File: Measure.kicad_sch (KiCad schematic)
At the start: 22 parts, among them U4 AD8210, U5 AD8210, U6 AD8210, U7 AD8210

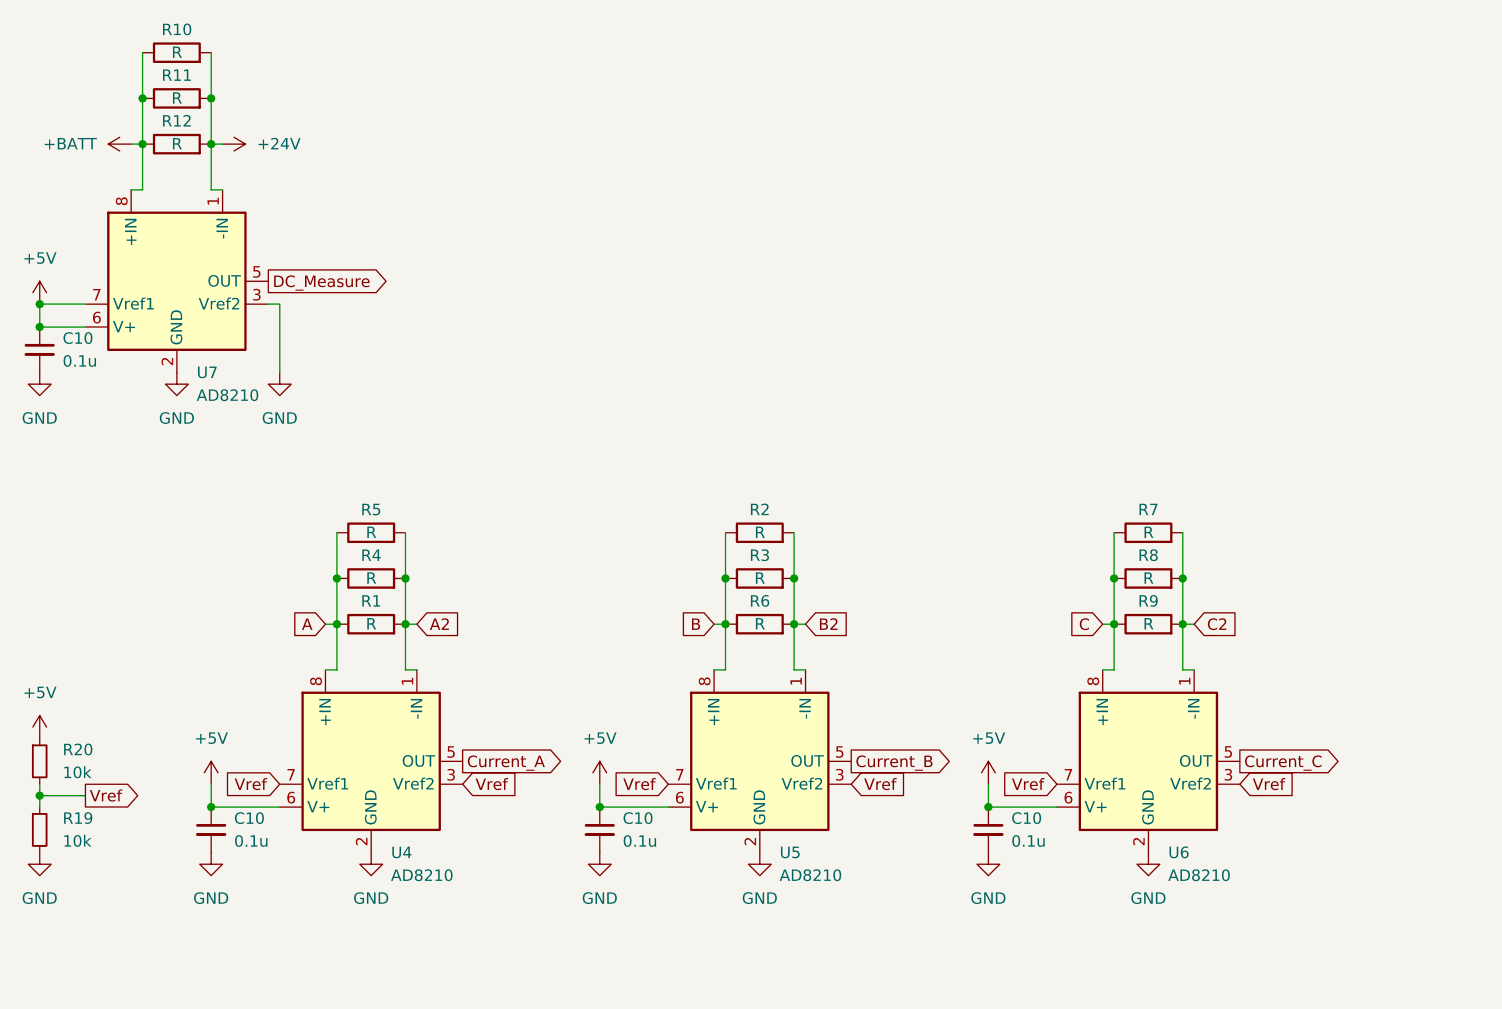
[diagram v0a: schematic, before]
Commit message: Добавил шунты
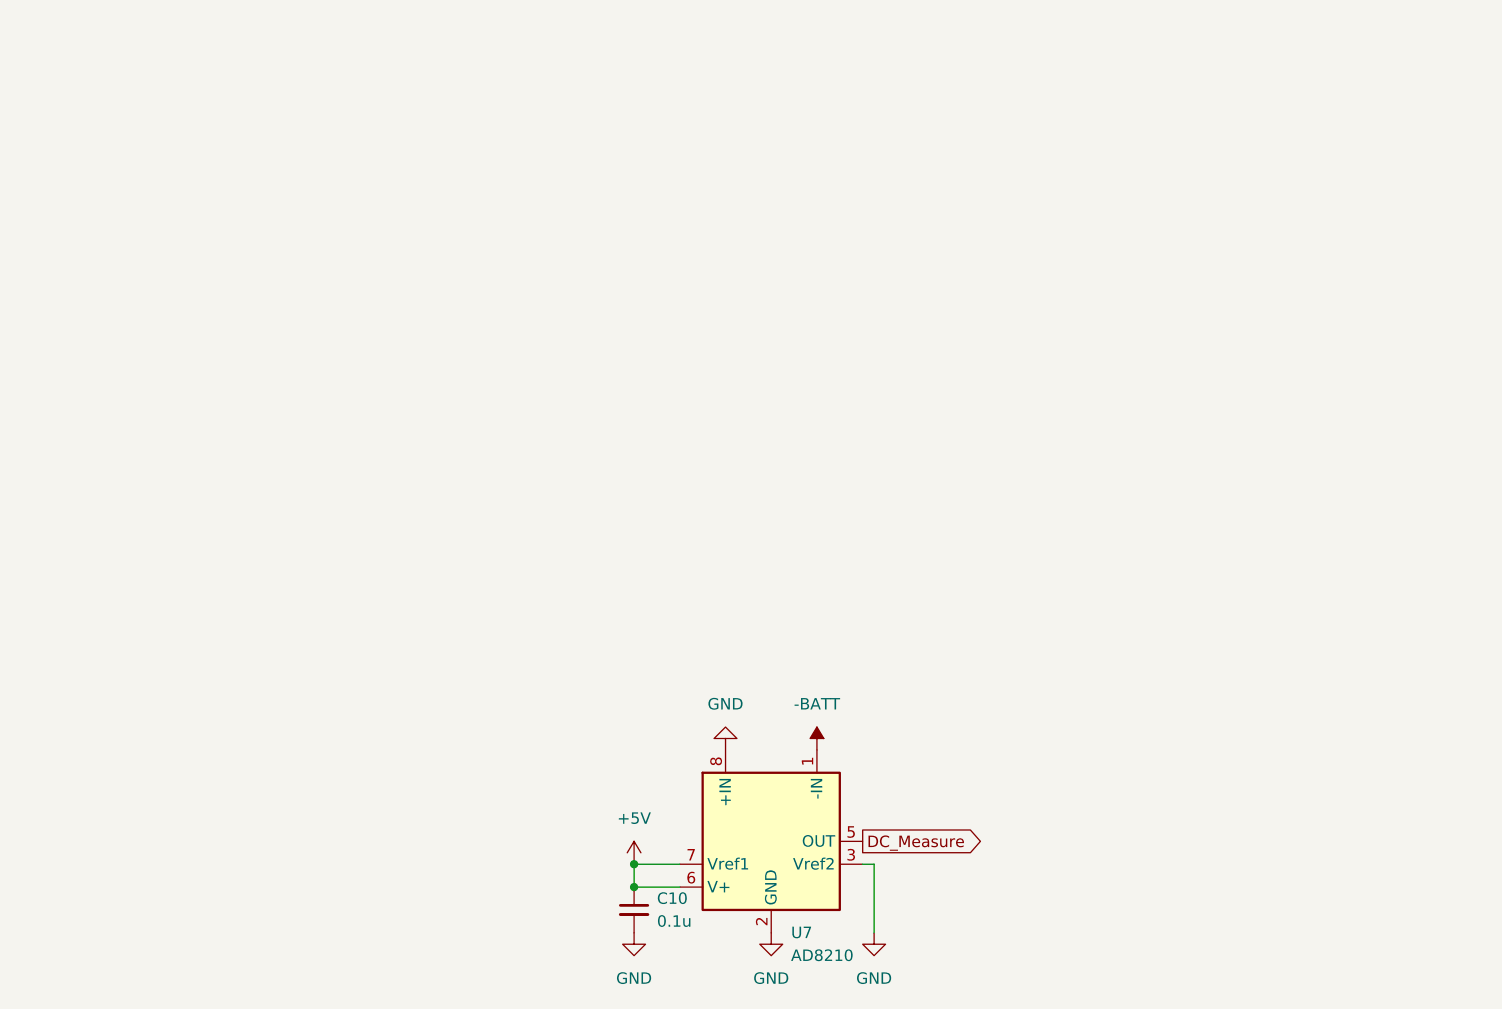
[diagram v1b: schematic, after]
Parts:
- removed C10 (x3): 0.1u, Capacitor_SMD:C_0805_2012Metric_Pad1.18x1.45mm_HandSolder, symbol Device:C_Small
- removed R1, R10, R11, R12, R2, R3, R4, R5, R6, R7, R8, R9: R, Resistor_SMD:R_2512_6332Metric_Pad1.40x3.35mm_HandSolder, symbol Device:R
- removed R19, R20: 10k, Resistor_SMD:R_0805_2012Metric_Pad1.20x1.40mm_HandSolder, symbol Device:R_Small
- removed U4, U5, U6: AD8210, Package_SO:SOIC-8_3.9x4.9mm_P1.27mm, symbol Amplifier_Current:AD8210
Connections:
- net +BATT is gone; now on net GND: U7.8 (+IN)
- net +24V renamed -BATT
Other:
- moved on the sheet: C10, U7

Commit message: Стартовый вариант
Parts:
- added C10: 0.1u, Capacitor_SMD:C_0805_2012Metric_Pad1.18x1.45mm_HandSolder, symbol Device:C_Small
- added C10 (x2): 56p, Capacitor_SMD:C_0805_2012Metric_Pad1.18x1.45mm_HandSolder, symbol Device:C_Small
- added R2, R3, R4, R5: 120, Resistor_SMD:R_0805_2012Metric_Pad1.20x1.40mm_HandSolder, symbol Device:R_Small
- added U1: LMV7239M5, Package_TO_SOT_SMD:SOT-353_SC-70-5, symbol Comparator:LMV7219M7
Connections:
- net +5V: now also C10.1, R3.2, U1.5 (V+)
- net DC_Measure: now also R5.2
- net GND: now also C10.2, C10.2, C10.2, R4.1, U1.2 (V-); no longer U7.8 (+IN)
- net -BATT renamed Shunt_2
- new net: C10.1, R5.1, U1.4 (-)
- new net: R3.1, R4.2, U1.3 (+)
- new net: R2.1, U1.1
- new net Enable: C10.1, R2.2
- new net Shunt_1: U7.8 (+IN)

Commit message: Стартовая версия
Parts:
- removed C10: 0.1u, Capacitor_SMD:C_0805_2012Metric_Pad1.18x1.45mm_HandSolder, symbol Device:C_Small
- removed C10: 56p, Capacitor_SMD:C_0805_2012Metric_Pad1.18x1.45mm_HandSolder, symbol Device:C_Small
- removed R2, R3, R4: 120, Resistor_SMD:R_0805_2012Metric_Pad1.20x1.40mm_HandSolder, symbol Device:R_Small
- removed U1: LMV7239M5, Package_TO_SOT_SMD:SOT-353_SC-70-5, symbol Comparator:LMV7219M7
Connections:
- net DC_Measure: now also C10.1, R5.1; no longer R5.2, U7.5 (OUT)
- new net: R5.2, U7.5 (OUT)
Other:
- moved on the sheet: R5

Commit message: Стартовая версия
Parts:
- renumbered R5 to R9
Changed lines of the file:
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@@
   (symbol (lib_id "Device:R_Small") (at 121.92 110.49 270) (unit 1)
     (in_bom yes) (on_board yes) (dnp no) (fields_autoplaced)
-    (property "Reference" "R5" (at 121.92 105.41 90)
+    (property "Reference" "R9" (at 121.92 105.41 90)
       (effects (font (size 1.27 1.27)))
     )
@@
       (project "Силовая плата"
         (path "/96c6fc92-8ec6-44f7-b0dc-9ad8f1acea09/1efb5faf-bb82-4ac6-a144-d6576b4720aa"
-          (reference "R5") (unit 1)
+          (reference "R9") (unit 1)
         )
       )
@@
         )
         (path "/96c6fc92-8ec6-44f7-b0dc-9ad8f1acea09/1efb5faf-bb82-4ac6-a144-d6576b4720aa"
-          (reference "U6") (unit 1)
+          (reference "U1") (unit 1)
         )
         (path "/96c6fc92-8ec6-44f7-b0dc-9ad8f1acea09/a27b443f-c036-4fd6-934c-6ea912709de0"
@@
         )
         (path "/96c6fc92-8ec6-44f7-b0dc-9ad8f1acea09/1efb5faf-bb82-4ac6-a144-d6576b4720aa"
-          (reference "C10") (unit 1)
+          (reference "C2") (unit 1)
         )
         (path "/96c6fc92-8ec6-44f7-b0dc-9ad8f1acea09/a27b443f-c036-4fd6-934c-6ea912709de0"
@@
         )
         (path "/96c6fc92-8ec6-44f7-b0dc-9ad8f1acea09/1efb5faf-bb82-4ac6-a144-d6576b4720aa"
-          (reference "C12") (unit 1)
+          (reference "C3") (unit 1)
         )
         (path "/96c6fc92-8ec6-44f7-b0dc-9ad8f1acea09/a27b443f-c036-4fd6-934c-6ea912709de0"
@@
         )
         (path "/96c6fc92-8ec6-44f7-b0dc-9ad8f1acea09/1efb5faf-bb82-4ac6-a144-d6576b4720aa"
+          (reference "#PWR09") (unit 1)
+        )
+        (path "/96c6fc92-8ec6-44f7-b0dc-9ad8f1acea09/a27b443f-c036-4fd6-934c-6ea912709de0"
+          (reference "#PWR029") (unit 1)
+        )
+      )
+    )
+  )
+  (symbol (lib_id "power:GND") (at 88.9 120.65 0) (unit 1)
+    (in_bom yes) (on_board yes) (dnp no) (fields_autoplaced)
+    (property "Reference" "#PWR011" (at 88.9 127 0)
+      (effects (font (size 1.27 1.27)) hide)
+    )
+    (property "Value" "GND" (at 88.9 125.73 0)
+      (effects (font (size 1.27 1.27)))
+    )
+    (property "Footprint" "" (at 88.9 120.65 0)
+      (effects (font (size 1.27 1.27)) hide)
+    )
+    (property "Datasheet" "" (at 88.9 120.65 0)
+      (effects (font (size 1.27 1.27)) hide)
+    )
+    (pin "1")
+    (instances
+      (project "Силовая плата"
+        (path "/96c6fc92-8ec6-44f7-b0dc-9ad8f1acea09"
+          (reference "#PWR011") (unit 1)
+        )
+        (path "/96c6fc92-8ec6-44f7-b0dc-9ad8f1acea09/1efb5faf-bb82-4ac6-a144-d6576b4720aa"
+          (reference "#PWR07") (unit 1)
+        )
+        (path "/96c6fc92-8ec6-44f7-b0dc-9ad8f1acea09/a27b443f-c036-4fd6-934c-6ea912709de0"
+          (reference "#PWR021") (unit 1)
+        )
+      )
+    )
+  )
+  (symbol (lib_id "power:GND") (at 129.54 120.65 0) (unit 1)
+    (in_bom yes) (on_board yes) (dnp no) (fields_autoplaced)
+    (property "Reference" "#PWR06" (at 129.54 127 0)
+      (effects (font (size 1.27 1.27)) hide)
+    )
+    (property "Value" "GND" (at 129.54 125.73 0)
+      (effects (font (size 1.27 1.27)))
+    )
+    (property "Footprint" "" (at 129.54 120.65 0)
+      (effects (font (size 1.27 1.27)) hide)
+    )
+    (property "Datasheet" "" (at 129.54 120.65 0)
+      (effects (font (size 1.27 1.27)) hide)
+    )
+    (pin "1")
+    (instances
+      (project "Силовая плата"
+        (path "/96c6fc92-8ec6-44f7-b0dc-9ad8f1acea09"
+          (reference "#PWR06") (unit 1)
+        )
+        (path "/96c6fc92-8ec6-44f7-b0dc-9ad8f1acea09/1efb5faf-bb82-4ac6-a144-d6576b4720aa"
           (reference "#PWR010") (unit 1)
         )
         (path "/96c6fc92-8ec6-44f7-b0dc-9ad8f1acea09/a27b443f-c036-4fd6-934c-6ea912709de0"
-          (reference "#PWR029") (unit 1)
-        )
-      )
-    )
-  )
-  (symbol (lib_id "power:GND") (at 88.9 120.65 0) (unit 1)
-    (in_bom yes) (on_board yes) (dnp no) (fields_autoplaced)
-    (property "Reference" "#PWR011" (at 88.9 127 0)
-      (effects (font (size 1.27 1.27)) hide)
-    )
-    (property "Value" "GND" (at 88.9 125.73 0)
-      (effects (font (size 1.27 1.27)))
-    )
-    (property "Footprint" "" (at 88.9 120.65 0)
-      (effects (font (size 1.27 1.27)) hide)
-    )
-    (property "Datasheet" "" (at 88.9 120.65 0)
-      (effects (font (size 1.27 1.27)) hide)
-    )
-    (pin "1")
-    (instances
-      (project "Силовая плата"
-        (path "/96c6fc92-8ec6-44f7-b0dc-9ad8f1acea09"
-          (reference "#PWR011") (unit 1)
-        )
-        (path "/96c6fc92-8ec6-44f7-b0dc-9ad8f1acea09/1efb5faf-bb82-4ac6-a144-d6576b4720aa"
-          (reference "#PWR04") (unit 1)
-        )
-        (path "/96c6fc92-8ec6-44f7-b0dc-9ad8f1acea09/a27b443f-c036-4fd6-934c-6ea912709de0"
-          (reference "#PWR021") (unit 1)
-        )
-      )
-    )
-  )
-  (symbol (lib_id "power:GND") (at 129.54 120.65 0) (unit 1)
-    (in_bom yes) (on_board yes) (dnp no) (fields_autoplaced)
-    (property "Reference" "#PWR06" (at 129.54 127 0)
-      (effects (font (size 1.27 1.27)) hide)
-    )
-    (property "Value" "GND" (at 129.54 125.73 0)
-      (effects (font (size 1.27 1.27)))
-    )
-    (property "Footprint" "" (at 129.54 120.65 0)
-      (effects (font (size 1.27 1.27)) hide)
-    )
-    (property "Datasheet" "" (at 129.54 120.65 0)
+          (reference "#PWR025") (unit 1)
+        )
+      )
+    )
+  )
+  (symbol (lib_id "power:GND") (at 104.14 120.65 0) (unit 1)
+    (in_bom yes) (on_board yes) (dnp no) (fields_autoplaced)
+    (property "Reference" "#PWR06" (at 104.14 127 0)
+      (effects (font (size 1.27 1.27)) hide)
+    )
+    (property "Value" "GND" (at 104.14 125.73 0)
+      (effects (font (size 1.27 1.27)))
+    )
+    (property "Footprint" "" (at 104.14 120.65 0)
+      (effects (font (size 1.27 1.27)) hide)
+    )
+    (property "Datasheet" "" (at 104.14 120.65 0)
       (effects (font (size 1.27 1.27)) hide)
     )
@@
         )
         (path "/96c6fc92-8ec6-44f7-b0dc-9ad8f1acea09/1efb5faf-bb82-4ac6-a144-d6576b4720aa"
-          (reference "#PWR014") (unit 1)
+          (reference "#PWR08") (unit 1)
         )
         (path "/96c6fc92-8ec6-44f7-b0dc-9ad8f1acea09/a27b443f-c036-4fd6-934c-6ea912709de0"
@@
     )
   )
-  (symbol (lib_id "power:GND") (at 104.14 120.65 0) (unit 1)
-    (in_bom yes) (on_board yes) (dnp no) (fields_autoplaced)
-    (property "Reference" "#PWR06" (at 104.14 127 0)
-      (effects (font (size 1.27 1.27)) hide)
-    )
-    (property "Value" "GND" (at 104.14 125.73 0)
-      (effects (font (size 1.27 1.27)))
-    )
-    (property "Footprint" "" (at 104.14 120.65 0)
-      (effects (font (size 1.27 1.27)) hide)
-    )
-    (property "Datasheet" "" (at 104.14 120.65 0)
-      (effects (font (size 1.27 1.27)) hide)
-    )
-    (pin "1")
-    (instances
-      (project "Силовая плата"
-        (path "/96c6fc92-8ec6-44f7-b0dc-9ad8f1acea09"
+  (symbol (lib_id "power:+5V") (at 88.9 113.03 0) (unit 1)
+    (in_bom yes) (on_board yes) (dnp no) (fields_autoplaced)
+    (property "Reference" "#PWR010" (at 88.9 116.84 0)
+      (effects (font (size 1.27 1.27)) hide)
+    )
+    (property "Value" "+5V" (at 88.9 107.95 0)
+      (effects (font (size 1.27 1.27)))
+    )
+    (property "Footprint" "" (at 88.9 113.03 0)
+      (effects (font (size 1.27 1.27)) hide)
+    )
+    (property "Datasheet" "" (at 88.9 113.03 0)
+      (effects (font (size 1.27 1.27)) hide)
+    )
+    (pin "1")
+    (instances
+      (project "Силовая плата"
+        (path "/96c6fc92-8ec6-44f7-b0dc-9ad8f1acea09"
+          (reference "#PWR010") (unit 1)
+        )
+        (path "/96c6fc92-8ec6-44f7-b0dc-9ad8f1acea09/1efb5faf-bb82-4ac6-a144-d6576b4720aa"
           (reference "#PWR06") (unit 1)
         )
-        (path "/96c6fc92-8ec6-44f7-b0dc-9ad8f1acea09/1efb5faf-bb82-4ac6-a144-d6576b4720aa"
-          (reference "#PWR08") (unit 1)
-        )
-        (path "/96c6fc92-8ec6-44f7-b0dc-9ad8f1acea09/a27b443f-c036-4fd6-934c-6ea912709de0"
-          (reference "#PWR025") (unit 1)
-        )
-      )
-    )
-  )
-  (symbol (lib_id "power:+5V") (at 88.9 113.03 0) (unit 1)
-    (in_bom yes) (on_board yes) (dnp no) (fields_autoplaced)
-    (property "Reference" "#PWR010" (at 88.9 116.84 0)
-      (effects (font (size 1.27 1.27)) hide)
-    )
-    (property "Value" "+5V" (at 88.9 107.95 0)
-      (effects (font (size 1.27 1.27)))
-    )
-    (property "Footprint" "" (at 88.9 113.03 0)
-      (effects (font (size 1.27 1.27)) hide)
-    )
-    (property "Datasheet" "" (at 88.9 113.03 0)
-      (effects (font (size 1.27 1.27)) hide)
-    )
-    (pin "1")
-    (instances
-      (project "Силовая плата"
-        (path "/96c6fc92-8ec6-44f7-b0dc-9ad8f1acea09"
-          (reference "#PWR010") (unit 1)
-        )
-        (path "/96c6fc92-8ec6-44f7-b0dc-9ad8f1acea09/1efb5faf-bb82-4ac6-a144-d6576b4720aa"
-          (reference "#PWR03") (unit 1)
-        )
-        (path "/96c6fc92-8ec6-44f7-b0dc-9ad8f1acea09/a27b443f-c036-4fd6-934c-6ea912709de0"
+        (path "/96c6fc92-8ec6-44f7-b0dc-9ad8f1acea09/a27b443f-c036-4fd6-934c-6ea912709de0"
